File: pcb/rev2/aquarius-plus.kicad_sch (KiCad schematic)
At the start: 169 parts, among them J1 Cassette in, J10 Audio out, J11 Hand controller 2, J12 ESP USB Host, J14 FPGA spare, J15 Expansion port, J16 ESP32 spare, J2 Cassette out, J3 TF-03A, J4 Printer, J5 Hand controller 1, J6 VGA, J7 DBG, J8 Power in, Q1 BC847C, Q2 BC847C, Q3 2N7002, SW1 SW_DPDT_x2, U1 XC6SLX9-2TQG144C, U10 IS61C5128AS-25QLI, U11 SN74CB3T3245PWR, U15 LDL1117S33R, U17 LD1117S12, U2 SN74CB3T3245PWR, U3 MAX3221ECPWR, U4 SN74CB3T3245PWR, U5 ESP32-S3-WROOM-1-N4R2, U6 SN74CB3T3245PWR, U7 Z84C0010AEG, U8 SN74AHCT1G125DBVR, U9 SN74AHCT1G125DBVR, X1 SX3M14.31818M20F30TNN

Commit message: Cleaned up PCB.
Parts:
- J10: renamed from J14; footprint Connector_PinHeader_2.54mm:PinHeader_2x05_P2.54mm_Vertical -> Connector_PinHeader_2.54mm:PinHeader_2x06_P2.54mm_Vertical; symbol Connector_Generic:Conn_02x05_Odd_Even -> Connector_Generic:Conn_02x06_Odd_Even
- J13: renamed from J16; footprint Connector_PinHeader_2.54mm:PinHeader_2x05_P2.54mm_Vertical -> Connector_PinHeader_2.54mm:PinHeader_2x07_P2.54mm_Vertical; symbol Connector_Generic:Conn_02x05_Odd_Even -> Connector_Generic:Conn_02x07_Odd_Even
- renumbered C48 to C1, C43 to C10, C40 to C11, C67 to C12, C64 to C13, C3 to C14, C17 to C15, C6 to C16, C12 to C17, C1 to C18, C7 to C19, C45 to C2, C26 to C20, C5 to C21, C2 to C22, C41 to C23, C44 to C24, C31 to C25, C38 to C26, C32 to C27, C39 to C28, C35 to C29, C49 to C3, C8 to C30, C28 to C31, C29 to C32, C10 to C33, C21 to C34, C25 to C35, C11 to C36, C24 to C37, C13 to C38, C30 to C39, C46 to C4, C19 to C40, C47 to C41, C14 to C42, C18 to C43, C20 to C44, C42 to C45, C4 to C46, C65 to C47, C62 to C48, C23 to C49, C61 to C5, C15 to C50, C27 to C51, C16 to C52, C22 to C53, C9 to C54, C34 to C56, C36 to C57, C37 to C58, C33 to C6, C54 to C7, C50 to C8, C51 to C9, D4 to D3, J8 to J1, J5 to J12, J12 to J2, J10 to J3, J6 to J4, J2 to J5, J1 to J6, J15 to J7, J4 to J8, J3 to J9, JP4 to JP1, JP5 to JP2, JP1 to JP3, J7 to JP4, R21 to R1, R45 to R10, R34 to R11, R38 to R12, R42 to R13, R46 to R14, R35 to R15, R39 to R16, R43 to R17, R15 to R18, R36 to R19, R23 to R2, R40 to R20, R44 to R21, R14 to R22, R52 to R23, R49 to R24, R51 to R25, R50 to R26, R48 to R27, R47 to R28, R28 to R29, R81 to R3, R32 to R30, R25 to R31, R26 to R32, R29 to R33, R30 to R34, R31 to R35, R102 to R36, R101 to R37, R53 to R38, R99 to R39, R71 to R4, R24 to R40, R20 to R41, R12 to R42, R19 to R43, R13 to R44, R18 to R45, R17 to R46, R16 to R47, R22 to R48, R27 to R49, R82 to R5, R2 to R50, R62 to R51, R61 to R52, R60 to R53, R59 to R54, R58 to R55, R57 to R56, R56 to R57, R55 to R58, R3 to R59, R72 to R6, R90 to R60, R89 to R61, R88 to R62, R87 to R63, R86 to R64, R85 to R65, R84 to R66, R83 to R67, R1 to R68, R54 to R69, R33 to R7, R37 to R8, R41 to R9, U8 to U1, U5 to U10, U15 to U11, U4 to U12, U10 to U13, U9 to U2, U17 to U3, U6 to U4, U3 to U5, U1 to U6, U11 to U8, U2 to U9
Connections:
- net AUDIO_L: now also U6.35 (B3_IO); no longer U6.22 (B3_IO_GCLK25)
- net AUDIO_R: now also U6.34 (B3_IO_VREF); no longer U6.21 (B3_IO_GCLK24)
- net BA14: now also U6.101 (B1_IO); no longer U6.79 (B1_IO)
- net BA15: now also U6.102 (B1_IO); no longer U6.80 (B1_IO)
- net BA16: now also U6.100 (B1_IO); no longer U6.78 (B1_IO)
- net BA17: now also U6.99 (B1_IO); no longer U6.75 (B1_IO_AWAKE)
- net BA18: now also U6.104 (B1_IO_VREF); no longer U6.81 (B1_IO)
- net CASSETTE_IN: now also U6.40 (B2_IO); no longer U6.24 (B3_IO_GCLK27)
- net CASSETTE_OUT: now also U6.38 (B2_IO); no longer U6.23 (B3_IO_GCLK26)
- net ESP_CTS: now also U6.44 (B2_IO); no longer U6.29 (B3_IO)
- net ESP_EXP7: now also J13.9 (Pin_9)
- net ESP_NOTIFY: now also U6.48 (B2_IO); no longer U6.34 (B3_IO_VREF)
- net ESP_RTS: now also U6.46 (B2_IO); no longer U6.32 (B3_IO)
- net ESP_RX: now also U6.45 (B2_IO); no longer U6.30 (B3_IO)
- net ESP_TX: now also U6.47 (B2_IO_VREF); no longer U6.33 (B3_IO)
- net FPGA_A0: now also U6.143 (B0_IO_VREF); no longer U6.134 (B0_IO_GCLK19)
- net FPGA_A1: now also U6.142 (B0_IO); no longer U6.133 (B0_IO_GCLK18)
- net FPGA_A10: now also U6.131 (B0_IO_GCLK16); no longer U6.119 (B0_IO)
- net FPGA_A11: now also U6.127 (B0_IO_GCLK15); no longer U6.118 (B0_IO)
- net FPGA_A12: now also U6.126 (B0_IO_GCLK14); no longer U6.117 (B0_IO)
- net FPGA_A13: now also U6.124 (B0_IO_GCLK13); no longer U6.116 (B0_IO)
- net FPGA_A14: now also U6.123 (B0_IO_GCLK12); no longer U6.115 (B0_IO)
- net FPGA_A15: now also U6.121 (B0_IO); no longer U6.114 (B0_IO)
- net FPGA_A2: now also U6.141 (B0_IO); no longer U6.132 (B0_IO_GCLK17)
- net FPGA_A3: now also U6.140 (B0_IO); no longer U6.131 (B0_IO_GCLK16)
- net FPGA_A4: now also U6.139 (B0_IO); no longer U6.127 (B0_IO_GCLK15)
- net FPGA_A5: now also U6.138 (B0_IO); no longer U6.126 (B0_IO_GCLK14)
- net FPGA_A6: now also U6.137 (B0_IO); no longer U6.124 (B0_IO_GCLK13)
- net FPGA_A7: now also U6.134 (B0_IO_GCLK19); no longer U6.123 (B0_IO_GCLK12)
- net FPGA_A8: now also U6.133 (B0_IO_GCLK18); no longer U6.121 (B0_IO)
- net FPGA_A9: now also U6.132 (B0_IO_GCLK17); no longer U6.120 (B0_IO_VREF)
- net FPGA_BUSACK#: now also U6.5 (B3_IO); no longer U6.87 (B1_IO_GCLK6)
- net FPGA_BUSREQ#: now also U6.6 (B3_IO); no longer U6.88 (B1_IO_GCLK7)
- net FPGA_CART_CE#: now also U6.2 (B3_IO); no longer U6.85 (B1_IO_GCLK5)
- net FPGA_D0: now also U6.120 (B0_IO_VREF); no longer U6.112 (B0_IO)
- net FPGA_D1: now also U6.119 (B0_IO); no longer U6.111 (B0_IO)
- net FPGA_D2: now also U6.118 (B0_IO); no longer U6.105 (B1_IO)
- net FPGA_D3: now also U6.117 (B0_IO); no longer U6.104 (B1_IO_VREF)
- net FPGA_D4: now also U6.116 (B0_IO); no longer U6.102 (B1_IO)
- net FPGA_D5: now also U6.115 (B0_IO); no longer U6.101 (B1_IO)
- net FPGA_D6: now also U6.114 (B0_IO); no longer U6.100 (B1_IO)
- net FPGA_D7: now also U6.112 (B0_IO); no longer U6.99 (B1_IO)
- net FPGA_EXP0: now also U6.66 (B2_IO)
- net FPGA_EXP1: now also U6.64 (B2_IO)
- net FPGA_EXP2: now also U6.62 (B2_IO)
- net FPGA_EXP3: now also U6.61 (B2_IO)
- net FPGA_EXP4: now also U6.59 (B2_IO)
- net FPGA_EXP5: now also U6.58 (B2_IO)
- net FPGA_EXP6: now also U6.57 (B2_IO)
- net FPGA_INT#: now also U6.8 (B3_IO); no longer U6.93 (B1_IO_GCLK9)
- net FPGA_IORQ#: now also U6.11 (B3_IO); no longer U6.97 (B1_IO)
- net FPGA_MREQ#: now also U6.12 (B3_IO); no longer U6.98 (B1_IO)
- net FPGA_PHI: now also U6.1 (B3_IO); no longer U6.84 (B1_IO_GCLK4)
- net FPGA_RD#: now also U6.10 (B3_IO); no longer U6.95 (B1_IO_GCLK11)
- net FPGA_RESET#: now also U6.7 (B3_IO); no longer U6.92 (B1_IO_GCLK8)
- net FPGA_WR#: now also U6.9 (B3_IO); no longer U6.94 (B1_IO_GCLK10)
- net GND: now also J10.12 (Pin_12), J13.13 (Pin_13), J13.14 (Pin_14); no longer J10.10 (Pin_10), J13.10 (Pin_10), J13.9 (Pin_9)
- net HC1_D00: now also U6.75 (B1_IO_AWAKE)
- net HC1_D01: now also U6.79 (B1_IO)
- net HC1_D02: now also U6.81 (B1_IO)
- net HC1_D03: now also U6.83 (B1_IO)
- net HC1_D04: now also U6.84 (B1_IO_GCLK4)
- net HC1_D05: now also U6.82 (B1_IO)
- net HC1_D06: now also U6.80 (B1_IO)
- net HC1_D07: now also U6.78 (B1_IO)
- net HC1_D08: now also U6.67 (B2_IO)
- net HC2_D00: now also U6.87 (B1_IO_GCLK6)
- net HC2_D01: now also U6.92 (B1_IO_GCLK8)
- net HC2_D02: now also U6.94 (B1_IO_GCLK10)
- net HC2_D03: now also U6.97 (B1_IO)
- net HC2_D04: now also U6.98 (B1_IO)
- net HC2_D05: now also U6.95 (B1_IO_GCLK11)
- net HC2_D06: now also U6.93 (B1_IO_GCLK9)
- net HC2_D07: now also U6.88 (B1_IO_GCLK7)
- net HC2_D08: now also U6.85 (B1_IO_GCLK5)
- net PRINTER_IN: now also U6.41 (B2_IO); no longer U6.26 (B3_IO)
- net PRINTER_OUT: now also U6.43 (B2_IO); no longer U6.27 (B3_IO)
- net RAM_CE#: now also U6.111 (B0_IO); no longer U6.83 (B1_IO)
- net RAM_WE#: now also U6.105 (B1_IO); no longer U6.82 (B1_IO)
- net VGA_B0: now also U6.16 (B3_IO_GCLK22); no longer U6.5 (B3_IO)
- net VGA_B1: now also U6.17 (B3_IO_GCLK23); no longer U6.6 (B3_IO)
- net VGA_B2: now also U6.21 (B3_IO_GCLK24); no longer U6.7 (B3_IO)
- net VGA_B3: now also U6.22 (B3_IO_GCLK25); no longer U6.8 (B3_IO)
- net VGA_G0: now also U6.23 (B3_IO_GCLK26); no longer U6.9 (B3_IO)
- net VGA_G1: now also U6.24 (B3_IO_GCLK27); no longer U6.10 (B3_IO)
- net VGA_G2: now also U6.26 (B3_IO); no longer U6.11 (B3_IO)
- net VGA_G3: now also U6.27 (B3_IO); no longer U6.12 (B3_IO)
- net VGA_HSYNC: now also U6.14 (B3_IO_GCLK20); no longer U6.1 (B3_IO)
- net VGA_R0: now also U6.29 (B3_IO); no longer U6.14 (B3_IO_GCLK20)
- net VGA_R1: now also U6.30 (B3_IO); no longer U6.15 (B3_IO_GCLK21)
- net VGA_R2: now also U6.32 (B3_IO); no longer U6.16 (B3_IO_GCLK22)
- net VGA_R3: now also U6.33 (B3_IO); no longer U6.17 (B3_IO_GCLK23)
- net VGA_VSYNC: now also U6.15 (B3_IO_GCLK21); no longer U6.2 (B3_IO)
- net USB_D-: now reaches J1.2 (D-), JP2.1 (A)
- net USB_D+: now reaches J1.3 (D+), JP1.1 (A)
- net ESP_EXP10: now reaches U10.11 (IO18)
- net ESP_EXP10: now also J13.12 (Pin_12)
- net ESP_EXP9: now reaches U10.28 (IO35)
- net ESP_EXP9: now also J13.11 (Pin_11)
- net ESP_EXP8: now reaches U10.29 (IO36)
- net ESP_EXP8: now also J13.10 (Pin_10)
- net FPGA_EXP9: now reaches U6.50 (B2_IO_GCLK30)
- net FPGA_EXP9: now also J10.11 (Pin_11)
- net FPGA_EXP8: now reaches U6.51 (B2_IO_GCLK31)
- net FPGA_EXP8: now also J10.10 (Pin_10)
- net FPGA_EXP7: now reaches U6.56 (B2_IO_GCLK1)
- net FPGA_EXP7: now also J10.9 (Pin_9)
- net ESP_USB_DM renamed ESP_USB_D-
- net ESP_USB_DP renamed ESP_USB_D+
- no-connect marks 20 -> 19
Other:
- moved on the sheet: H1, H2, H3, H4, J7, JP1, JP2

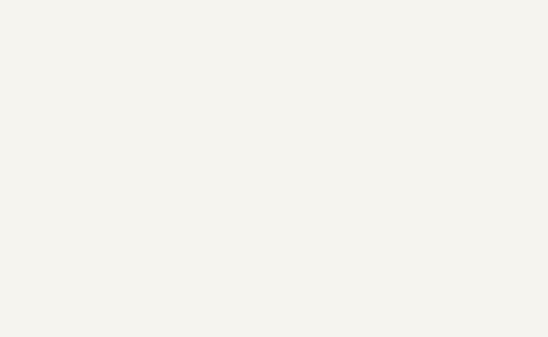
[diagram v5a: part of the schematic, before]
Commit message: Added fiducials.
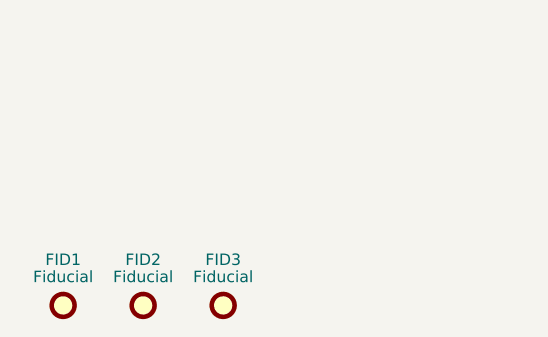
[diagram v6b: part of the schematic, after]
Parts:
- added FID1, FID2, FID3: Fiducial, Fiducial:Fiducial_1mm_Mask2mm, symbol Mechanical:Fiducial
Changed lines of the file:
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@@
+    )
+  )
+  (symbol (lib_id "Mechanical:Fiducial") (at 26.67 403.86 0) (unit 1)
+    (in_bom no) (on_board yes) (dnp no)
+    (property "Reference" "FID2" (at 26.67 398.78 0)
+      (effects (font (size 1.27 1.27)))
+    )
+    (property "Value" "Fiducial" (at 26.67 400.685 0)
+      (effects (font (size 1.27 1.27)))
+    )
+    (property "Footprint" "Fiducial:Fiducial_1mm_Mask2mm" (at 26.67 403.86 0)
+      (effects (font (size 1.27 1.27)) hide)
+    )
+    (property "Datasheet" "~" (at 26.67 403.86 0)
+      (effects (font (size 1.27 1.27)) hide)
+    )
+    (instances
+      (project "aquarius-plus"
+        (path "/e63e39d7-6ac0-4ffd-8aa3-1841a4541b55"
+          (reference "FID2") (unit 1)
+        )
+      )
     )
   )
@@
     )
   )
+  (symbol (lib_id "Mechanical:Fiducial") (at 17.78 403.86 0) (unit 1)
+    (in_bom no) (on_board yes) (dnp no)
+    (property "Reference" "FID1" (at 17.78 398.78 0)
+      (effects (font (size 1.27 1.27)))
+    )
+    (property "Value" "Fiducial" (at 17.78 400.685 0)
+      (effects (font (size 1.27 1.27)))
+    )
+    (property "Footprint" "Fiducial:Fiducial_1mm_Mask2mm" (at 17.78 403.86 0)
+      (effects (font (size 1.27 1.27)) hide)
+    )
+    (property "Datasheet" "~" (at 17.78 403.86 0)
+      (effects (font (size 1.27 1.27)) hide)
+    )
+    (instances
+      (project "aquarius-plus"
+        (path "/e63e39d7-6ac0-4ffd-8aa3-1841a4541b55"
+          (reference "FID1") (unit 1)
+        )
+      )
+    )
+  )
   (symbol (lib_id "Device:C_Small") (at 44.45 287.02 0) (unit 1)
     (in_bom yes) (on_board yes) (dnp no) (fields_autoplaced)
@@
         )
       )
+    )
+  )
+  (symbol (lib_id "Mechanical:Fiducial") (at 35.56 403.86 0) (unit 1)
+    (in_bom no) (on_board yes) (dnp no)
+    (property "Reference" "FID3" (at 35.56 398.78 0)
+      (effects (font (size 1.27 1.27)))
+    )
+    (property "Value" "Fiducial" (at 35.56 400.685 0)
+      (effects (font (size 1.27 1.27)))
+    )
+    (property "Footprint" "Fiducial:Fiducial_1mm_Mask2mm" (at 35.56 403.86 0)
+      (effects (font (size 1.27 1.27)) hide)
+    )
+    (property "Datasheet" "~" (at 35.56 403.86 0)
+      (effects (font (size 1.27 1.27)) hide)
+    )
+    (instances
+      (project "aquarius-plus"
+        (path "/e63e39d7-6ac0-4ffd-8aa3-1841a4541b55"
+          (reference "FID3") (unit 1)
+        )
+      )

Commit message: Update aquarius-plus.kicad_sch
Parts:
- J3, J5, J6, J8: footprint Connector_Audio:Jack_3.5mm_CUI_SJ-3523-SMT_Horizontal -> aquarius-plus:C2884998
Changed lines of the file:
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@@
       (effects (font (size 1.27 1.27)) (justify right))
     )
-    (property "Footprint" "Connector_Audio:Jack_3.5mm_CUI_SJ-3523-SMT_Horizontal" (at 170.18 201.93 0)
+    (property "Footprint" "aquarius-plus:C2884998" (at 170.18 201.93 0)
       (effects (font (size 1.27 1.27)) hide)
     )
@@
       (effects (font (size 1.27 1.27)) (justify right))
     )
-    (property "Footprint" "Connector_Audio:Jack_3.5mm_CUI_SJ-3523-SMT_Horizontal" (at 144.78 284.48 0)
+    (property "Footprint" "aquarius-plus:C2884998" (at 144.78 284.48 0)
       (effects (font (size 1.27 1.27)) hide)
     )
@@
       (effects (font (size 1.27 1.27)) (justify right))
     )
-    (property "Footprint" "Connector_Audio:Jack_3.5mm_CUI_SJ-3523-SMT_Horizontal" (at 113.03 313.69 0)
+    (property "Footprint" "aquarius-plus:C2884998" (at 113.03 313.69 0)
       (effects (font (size 1.27 1.27)) hide)
     )
@@
       (effects (font (size 1.27 1.27)) (justify right))
     )
-    (property "Footprint" "Connector_Audio:Jack_3.5mm_CUI_SJ-3523-SMT_Horizontal" (at 297.18 179.07 0)
+    (property "Footprint" "aquarius-plus:C2884998" (at 297.18 179.07 0)
       (effects (font (size 1.27 1.27)) hide)
     )

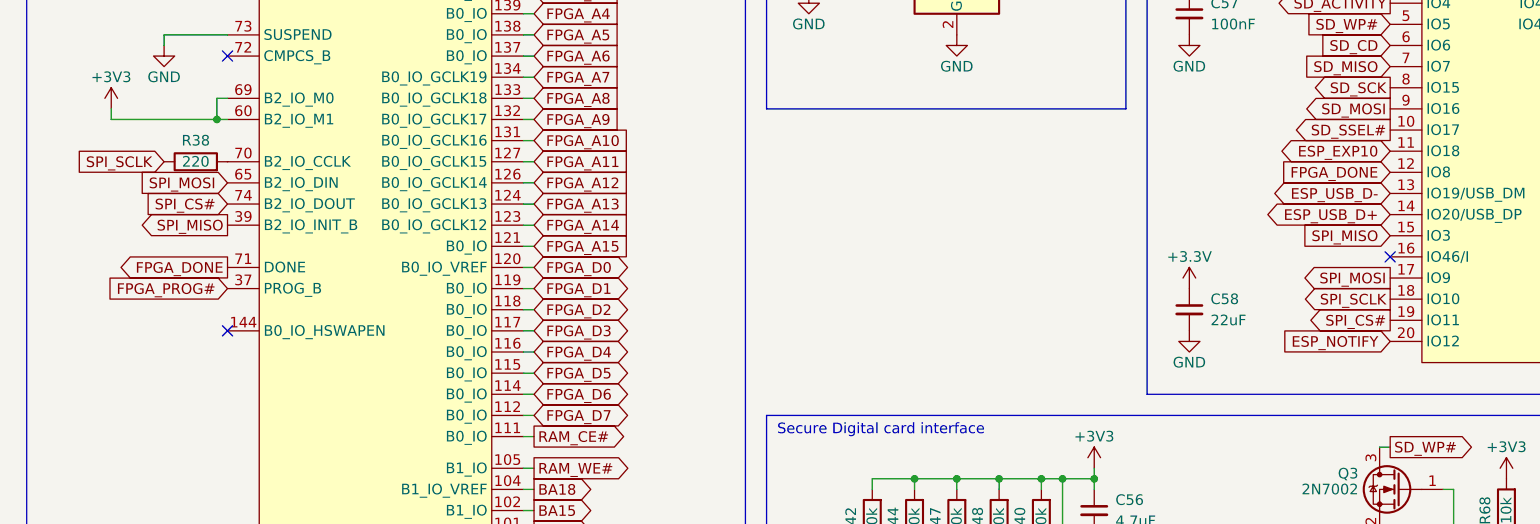
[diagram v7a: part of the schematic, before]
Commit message: Renaming SPI nets to match the software.
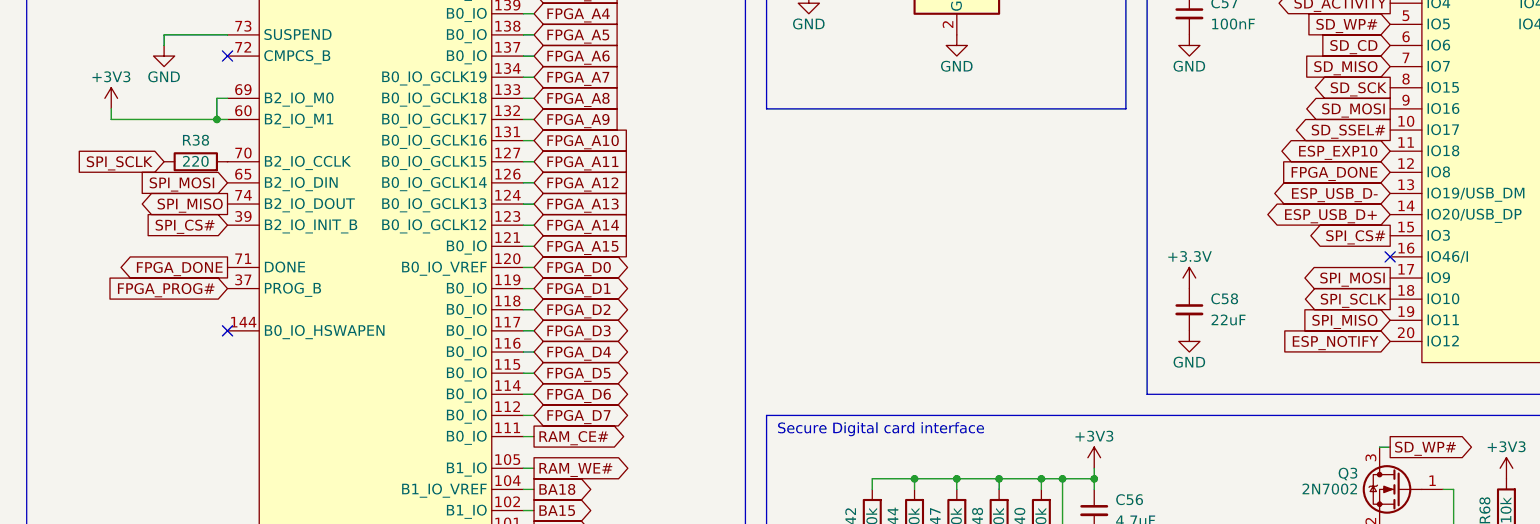
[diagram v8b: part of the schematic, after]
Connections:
- net SPI_CS#: now also U10.15 (IO3), U6.39 (B2_IO_INIT_B); no longer U10.19 (IO11), U6.74 (B2_IO_DOUT)
- net SPI_MISO: now also U10.19 (IO11), U6.74 (B2_IO_DOUT); no longer U10.15 (IO3), U6.39 (B2_IO_INIT_B)
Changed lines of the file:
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@@
     )
   )
-  (global_label "SPI_MISO" (shape output) (at 38.1 60.96 180) (fields_autoplaced)
-    (effects (font (size 1.27 1.27)) (justify right))
-    (property "Intersheetrefs" "${INTERSHEET_REFS}" (at 26.5461 60.96 0)
+  (global_label "SPI_CS#" (shape input) (at 38.1 60.96 180) (fields_autoplaced)
+    (effects (font (size 1.27 1.27)) (justify right))
+    (property "Intersheetrefs" "${INTERSHEET_REFS}" (at 27.3928 60.96 0)
       (effects (font (size 1.27 1.27)) (justify right) hide)
     )
@@
     )
   )
-  (global_label "SPI_MISO" (shape input) (at 177.8 62.23 180) (fields_autoplaced)
-    (effects (font (size 1.27 1.27)) (justify right))
-    (property "Intersheetrefs" "${INTERSHEET_REFS}" (at 166.7388 62.1506 0)
+  (global_label "SPI_CS#" (shape output) (at 177.8 62.23 180) (fields_autoplaced)
+    (effects (font (size 1.27 1.27)) (justify right))
+    (property "Intersheetrefs" "${INTERSHEET_REFS}" (at 167.0928 62.23 0)
       (effects (font (size 1.27 1.27)) (justify right) hide)
     )
@@
     )
   )
-  (global_label "SPI_CS#" (shape input) (at 38.1 58.42 180) (fields_autoplaced)
-    (effects (font (size 1.27 1.27)) (justify right))
-    (property "Intersheetrefs" "${INTERSHEET_REFS}" (at 27.8855 58.3406 0)
+  (global_label "SPI_MISO" (shape output) (at 38.1 58.42 180) (fields_autoplaced)
+    (effects (font (size 1.27 1.27)) (justify right))
+    (property "Intersheetrefs" "${INTERSHEET_REFS}" (at 26.5461 58.42 0)
       (effects (font (size 1.27 1.27)) (justify right) hide)
     )
@@
     )
   )
-  (global_label "SPI_CS#" (shape output) (at 177.8 72.39 180) (fields_autoplaced)
-    (effects (font (size 1.27 1.27)) (justify right))
-    (property "Intersheetrefs" "${INTERSHEET_REFS}" (at 167.5855 72.3106 0)
-      (effects (font (size 1.27 1.27)) (justify right) hide)
-    )
+  (global_label "SPI_MISO" (shape input) (at 177.8 72.39 180) (fields_autoplaced)
+    (effects (font (size 1.27 1.27)) (justify right))
+    (property "Intersheetrefs" "${INTERSHEET_REFS}" (at 166.2461 72.39 0)
+      (effects (font (size 1.27 1.27)) (justify right) hide)
+    )
